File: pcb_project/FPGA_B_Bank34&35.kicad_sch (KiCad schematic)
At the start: 6 parts, among them U1 XC7A100T-FTG256, Y3 XLH736025.175000I

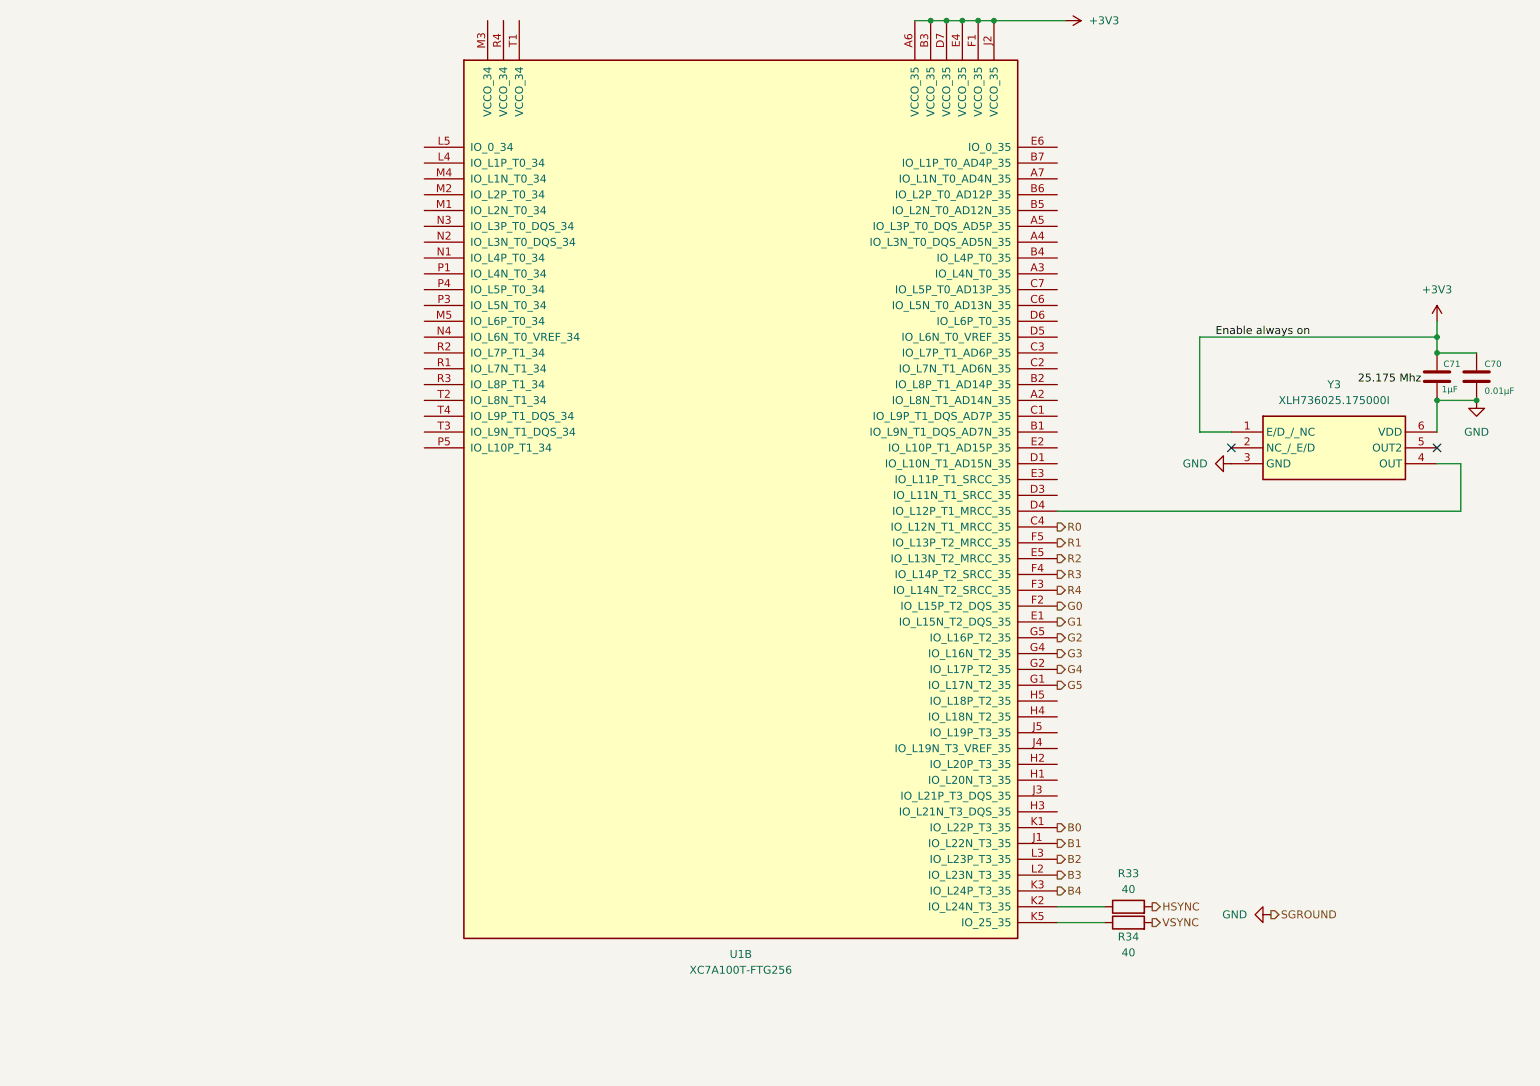
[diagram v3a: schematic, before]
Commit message: Add FPGA configuration LED's, config pins, no connect symbols
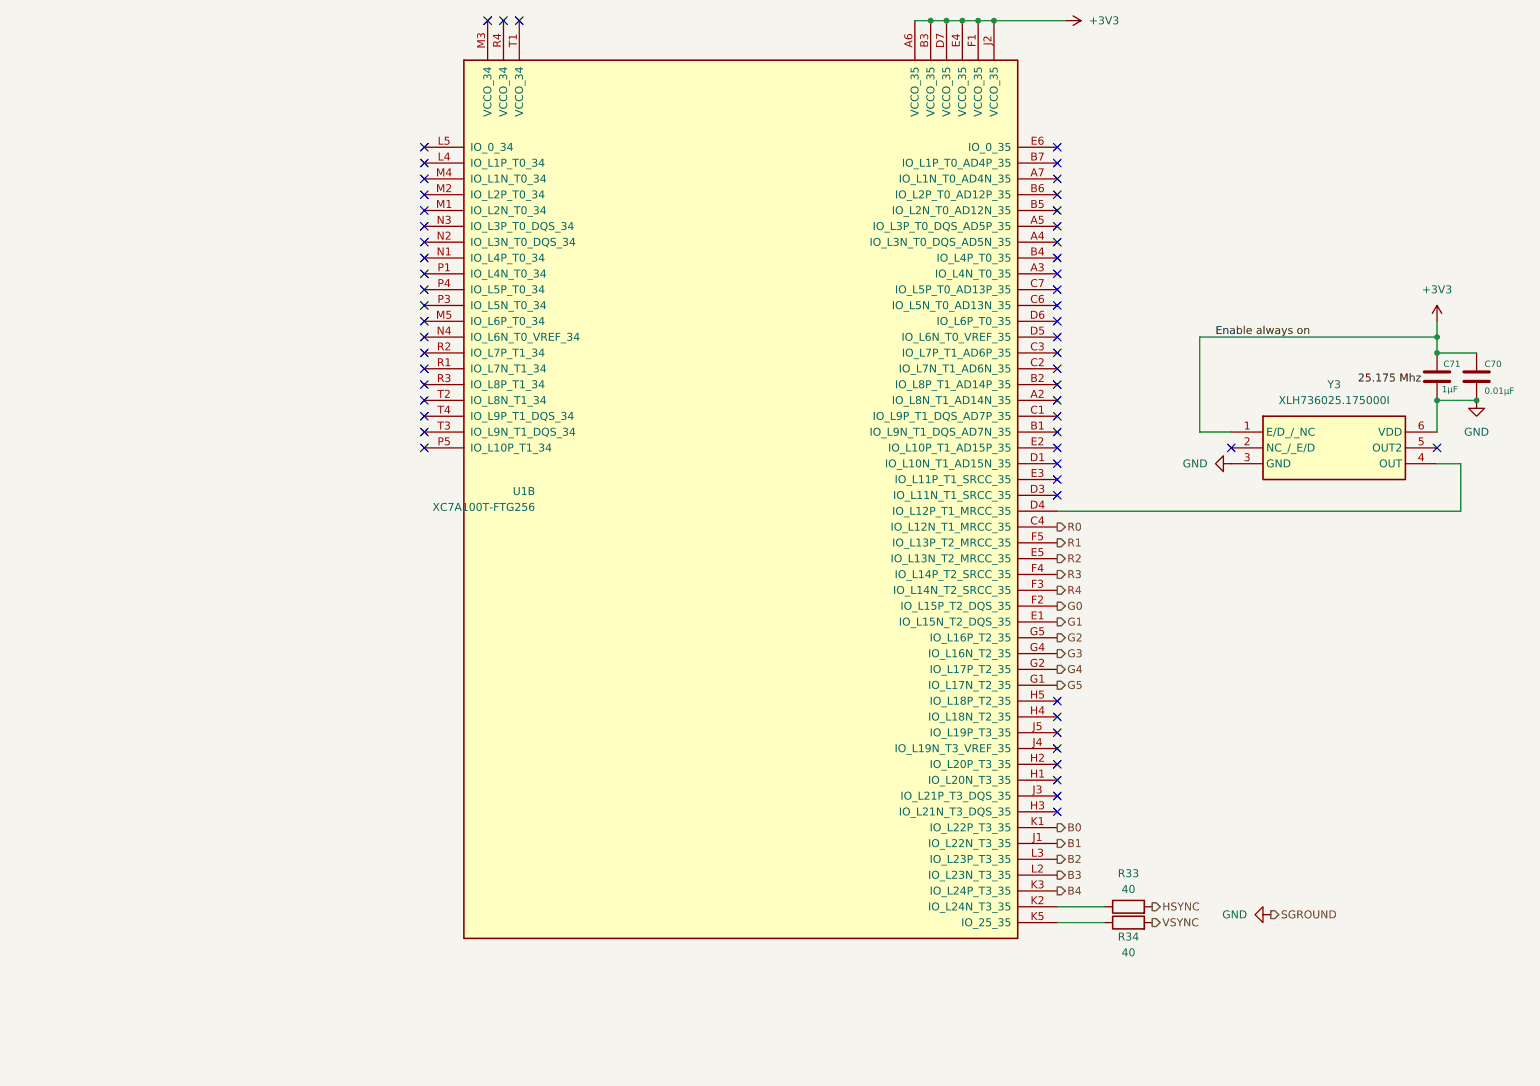
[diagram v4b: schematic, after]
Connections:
- no-connect marks 2 -> 56
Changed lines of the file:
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@@
+	)
+	(no_connect
+		(at 196.85 80.01)
+	)
+	(no_connect
+		(at 196.85 62.23)
+	)
+	(no_connect
+		(at 196.85 59.69)
+	)
+	(no_connect
+		(at 95.25 54.61)
+	)
+	(no_connect
+		(at 95.25 39.37)
+	)
+	(no_connect
+		(at 196.85 36.83)
+	)
+	(no_connect
+		(at 95.25 46.99)
+	)
+	(no_connect
+		(at 95.25 62.23)
+	)
+	(no_connect
+		(at 196.85 39.37)
+	)
+	(no_connect
+		(at 95.25 57.15)
+	)
+	(no_connect
+		(at 196.85 85.09)
+	)
+	(no_connect
+		(at 95.25 82.55)
+	)
+	(no_connect
+		(at 196.85 57.15)
+	)
+	(no_connect
+		(at 196.85 74.93)
+	)
+	(no_connect
+		(at 196.85 69.85)
+	)
+	(no_connect
+		(at 196.85 67.31)
+	)
+	(no_connect
+		(at 196.85 87.63)
+	)
+	(no_connect
+		(at 196.85 54.61)
+	)
+	(no_connect
+		(at 107.95 13.97)
+	)
+	(no_connect
+		(at 196.85 90.17)
+	)
+	(no_connect
+		(at 196.85 44.45)
+	)
+	(no_connect
+		(at 196.85 52.07)
+	)
+	(no_connect
+		(at 196.85 72.39)
+	)
+	(no_connect
+		(at 196.85 133.35)
+	)
+	(no_connect
+		(at 196.85 77.47)
+	)
+	(no_connect
+		(at 95.25 36.83)
+	)
+	(no_connect
+		(at 196.85 46.99)
+	)
+	(no_connect
+		(at 196.85 140.97)
+	)
+	(no_connect
+		(at 196.85 130.81)
+	)
+	(no_connect
+		(at 95.25 69.85)
+	)
+	(no_connect
+		(at 95.25 77.47)
+	)
+	(no_connect
+		(at 105.41 13.97)
 	)
 	(no_connect
@@
 	)
 	(no_connect
+		(at 196.85 49.53)
+	)
+	(no_connect
+		(at 196.85 128.27)
+	)
+	(no_connect
+		(at 196.85 34.29)
+	)
+	(no_connect
+		(at 196.85 64.77)
+	)
+	(no_connect
+		(at 196.85 135.89)
+	)
+	(no_connect
+		(at 95.25 72.39)
+	)
+	(no_connect
+		(at 95.25 59.69)
+	)
+	(no_connect
+		(at 196.85 41.91)
+	)
+	(no_connect
+		(at 95.25 80.01)
+	)
+	(no_connect
+		(at 196.85 123.19)
+	)
+	(no_connect
+		(at 95.25 49.53)
+	)
+	(no_connect
+		(at 196.85 125.73)
+	)
+	(no_connect
+		(at 95.25 34.29)
+	)
+	(no_connect
+		(at 95.25 64.77)
+	)
+	(no_connect
+		(at 196.85 82.55)
+	)
+	(no_connect
+		(at 95.25 74.93)
+	)
+	(no_connect
+		(at 95.25 67.31)
+	)
+	(no_connect
+		(at 110.49 13.97)
+	)
+	(no_connect
+		(at 196.85 138.43)
+	)
+	(no_connect
+		(at 95.25 44.45)
+	)
+	(no_connect
 		(at 224.79 82.55)
+	)
+	(no_connect
+		(at 95.25 41.91)
+	)
+	(no_connect
+		(at 95.25 52.07)
 	)
 	(wire
@@
 		(fields_autoplaced yes)
 		(property "Reference" "U1"
-			(at 146.05 163.83 0)
-			(effects
-				(font
-					(size 1.27 1.27)
-				)
+			(at 113.03 89.5349 0)
+			(effects
+				(font
+					(size 1.27 1.27)
+				)
+				(justify right)
 			)
 		)
 		(property "Value" "XC7A100T-FTG256"
-			(at 146.05 166.37 0)
-			(effects
-				(font
-					(size 1.27 1.27)
-				)
+			(at 113.03 92.0749 0)
+			(effects
+				(font
+					(size 1.27 1.27)
+				)
+				(justify right)
 			)
 		)
@@
 		)
 		(instances
-			(project "pcb_project"
+			(project ""
+				(path "/98f80f66-4595-4d0f-90ca-59b2db6f447b/8bdc4eb6-105b-4ccb-b86f-5b5221dfef47"
+					(reference "U1")
+					(unit 2)
+				)
 				(path "/98f80f66-4595-4d0f-90ca-59b2db6f447b/8bdc4eb6-105b-4ccb-b86f-5b5221dfef47/1311c77a-2e60-4e70-8492-84cf53095df7"
 					(reference "U1")

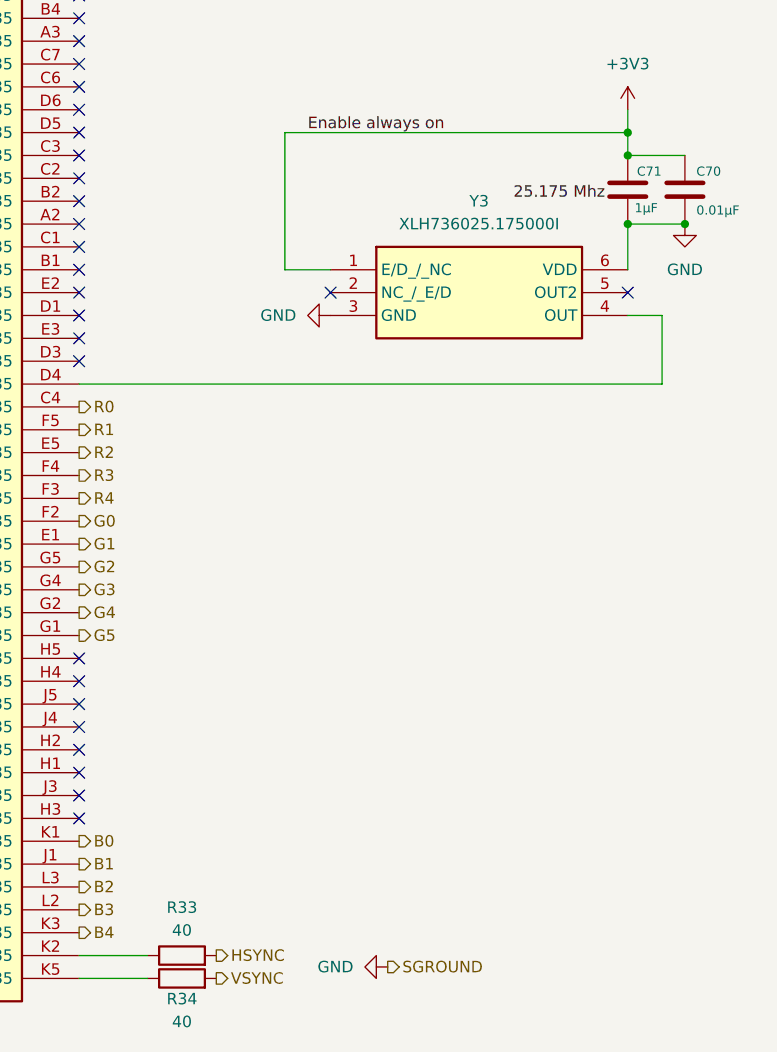
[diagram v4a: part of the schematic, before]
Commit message: ERC fixes, some remain
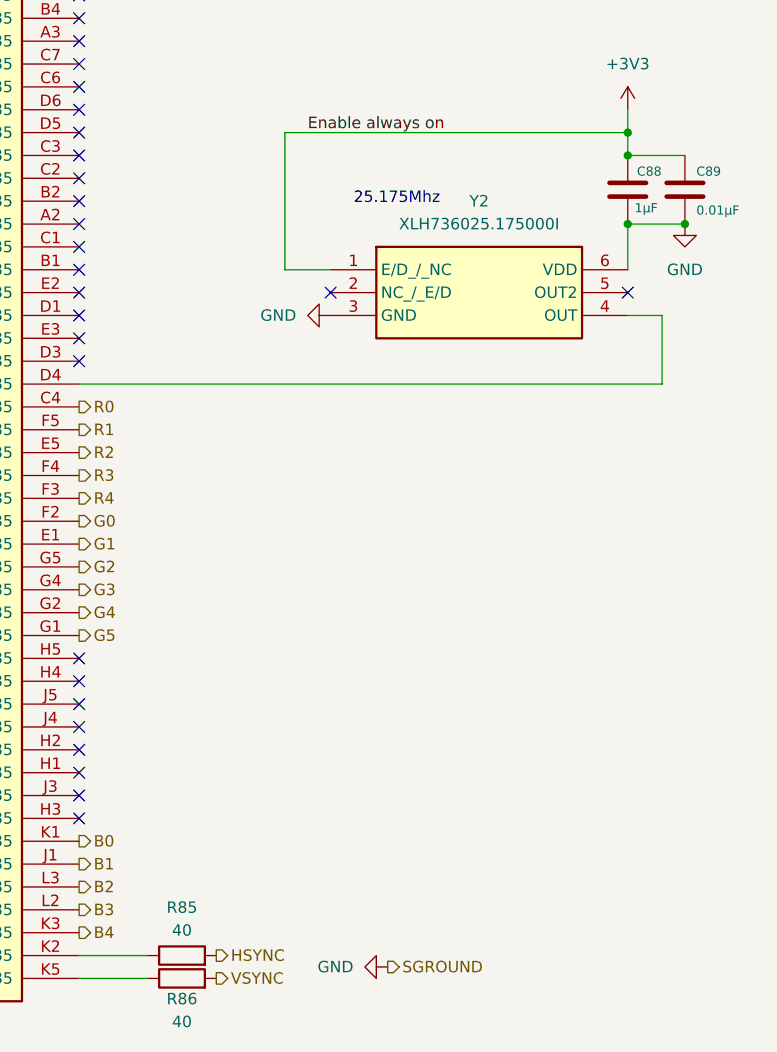
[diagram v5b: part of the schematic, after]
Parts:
- renumbered C71 to C88, C70 to C89, R33 to R85, R34 to R86, Y3 to Y2
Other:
- note added: "25.175Mhz"
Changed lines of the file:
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@@
 	(generator_version "9.0")
 	(paper "A4")
+	(text "25.175Mhz"
+		(exclude_from_sim no)
+		(at 232.156 72.136 0)
+		(effects
+			(font
+				(size 1.27 1.27)
+			)
+		)
+	)
 	(junction
 		(at 176.53 13.97)
@@
 			(width 0)
 			(type default)
-		)
-	)
-	(label "25.175 Mhz"
-		(at 245.11 72.39 0)
-		(effects
-			(font
-				(size 1.27 1.27)
-			)
-			(justify left bottom)
 		)
 	)
@@
 		(dnp no)
 		(fields_autoplaced yes)
-		(property "Reference" "#PWR014"
+		(property "Reference" "#PWR0116"
 			(at 218.44 85.09 0)
 			(effects
@@
 			(project ""
 				(path "/98f80f66-4595-4d0f-90ca-59b2db6f447b/8bdc4eb6-105b-4ccb-b86f-5b5221dfef47/1311c77a-2e60-4e70-8492-84cf53095df7"
-					(reference "#PWR014")
+					(reference "#PWR0116")
 					(unit 1)
 				)
@@
 		(dnp no)
 		(fields_autoplaced yes)
-		(property "Reference" "#PWR085"
+		(property "Reference" "#PWR0119"
 			(at 264.16 81.28 0)
 			(effects
@@
 			(project ""
 				(path "/98f80f66-4595-4d0f-90ca-59b2db6f447b/8bdc4eb6-105b-4ccb-b86f-5b5221dfef47/1311c77a-2e60-4e70-8492-84cf53095df7"
-					(reference "#PWR085")
+					(reference "#PWR0119")
 					(unit 1)
 				)
@@
 		(dnp no)
 		(fields_autoplaced yes)
-		(property "Reference" "#PWR017"
+		(property "Reference" "#PWR0118"
 			(at 257.81 66.04 0)
 			(effects
@@
 			(project ""
 				(path "/98f80f66-4595-4d0f-90ca-59b2db6f447b/8bdc4eb6-105b-4ccb-b86f-5b5221dfef47/1311c77a-2e60-4e70-8492-84cf53095df7"
-					(reference "#PWR017")
+					(reference "#PWR0118")
 					(unit 1)
 				)
@@
 		(dnp no)
 		(fields_autoplaced yes)
-		(property "Reference" "#PWR087"
+		(property "Reference" "#PWR0115"
 			(at 194.31 13.97 0)
 			(effects
@@
 			(project ""
 				(path "/98f80f66-4595-4d0f-90ca-59b2db6f447b/8bdc4eb6-105b-4ccb-b86f-5b5221dfef47/1311c77a-2e60-4e70-8492-84cf53095df7"
-					(reference "#PWR087")
+					(reference "#PWR0115")
 					(unit 1)
 				)
@@
 		(on_board yes)
 		(dnp no)
-		(property "Reference" "R33"
+		(property "Reference" "R85"
 			(at 208.28 150.876 90)
 			(effects
@@
 			(project ""
 				(path "/98f80f66-4595-4d0f-90ca-59b2db6f447b/8bdc4eb6-105b-4ccb-b86f-5b5221dfef47/1311c77a-2e60-4e70-8492-84cf53095df7"
-					(reference "R33")
+					(reference "R85")
 					(unit 1)
 				)
@@
 		(on_board yes)
 		(dnp no)
-		(property "Reference" "C70"
+		(property "Reference" "C89"
 			(at 265.43 69.088 0)
 			(effects
@@
 			(project ""
 				(path "/98f80f66-4595-4d0f-90ca-59b2db6f447b/8bdc4eb6-105b-4ccb-b86f-5b5221dfef47/1311c77a-2e60-4e70-8492-84cf53095df7"
-					(reference "C70")
+					(reference "C89")
 					(unit 1)
 				)
@@
 		(on_board yes)
 		(dnp no)
-		(property "Reference" "C71"
+		(property "Reference" "C88"
 			(at 258.826 69.088 0)
 			(effects
@@
 			(project "pcb_project"
 				(path "/98f80f66-4595-4d0f-90ca-59b2db6f447b/8bdc4eb6-105b-4ccb-b86f-5b5221dfef47/1311c77a-2e60-4e70-8492-84cf53095df7"
-					(reference "C71")
+					(reference "C88")
 					(unit 1)
 				)
@@
 		(on_board yes)
 		(dnp no)
-		(property "Reference" "R34"
+		(property "Reference" "R86"
 			(at 208.28 161.036 90)
 			(effects
@@
 			(project ""
 				(path "/98f80f66-4595-4d0f-90ca-59b2db6f447b/8bdc4eb6-105b-4ccb-b86f-5b5221dfef47/1311c77a-2e60-4e70-8492-84cf53095df7"
-					(reference "R34")
+					(reference "R86")
 					(unit 1)
 				)
@@
 		(dnp no)
 		(fields_autoplaced yes)
-		(property "Reference" "#PWR088"
+		(property "Reference" "#PWR0117"
 			(at 224.79 157.48 0)
 			(effects
@@
 			(project ""
 				(path "/98f80f66-4595-4d0f-90ca-59b2db6f447b/8bdc4eb6-105b-4ccb-b86f-5b5221dfef47/1311c77a-2e60-4e70-8492-84cf53095df7"
-					(reference "#PWR088")
+					(reference "#PWR0117")
 					(unit 1)
 				)
@@
 		(dnp no)
 		(fields_autoplaced yes)
-		(property "Reference" "Y3"
+		(property "Reference" "Y2"
 			(at 241.3 72.39 0)
 			(effects
@@
 			(project ""
 				(path "/98f80f66-4595-4d0f-90ca-59b2db6f447b/8bdc4eb6-105b-4ccb-b86f-5b5221dfef47/1311c77a-2e60-4e70-8492-84cf53095df7"
-					(reference "Y3")
+					(reference "Y2")
 					(unit 1)
 				)

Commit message: Fix JTAG connector, add pullups (FPGA has internal pullups as well), add some capacitor footprints
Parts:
- Y2: footprint XLH730003580000I -> Project_Footprints:XLH730003580000I
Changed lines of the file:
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@@
 			)
 		)
-		(property "Footprint" "XLH730003580000I"
+		(property "Footprint" "Project_Footprints:XLH730003580000I"
 			(at 254 174.93 0)
 			(effects

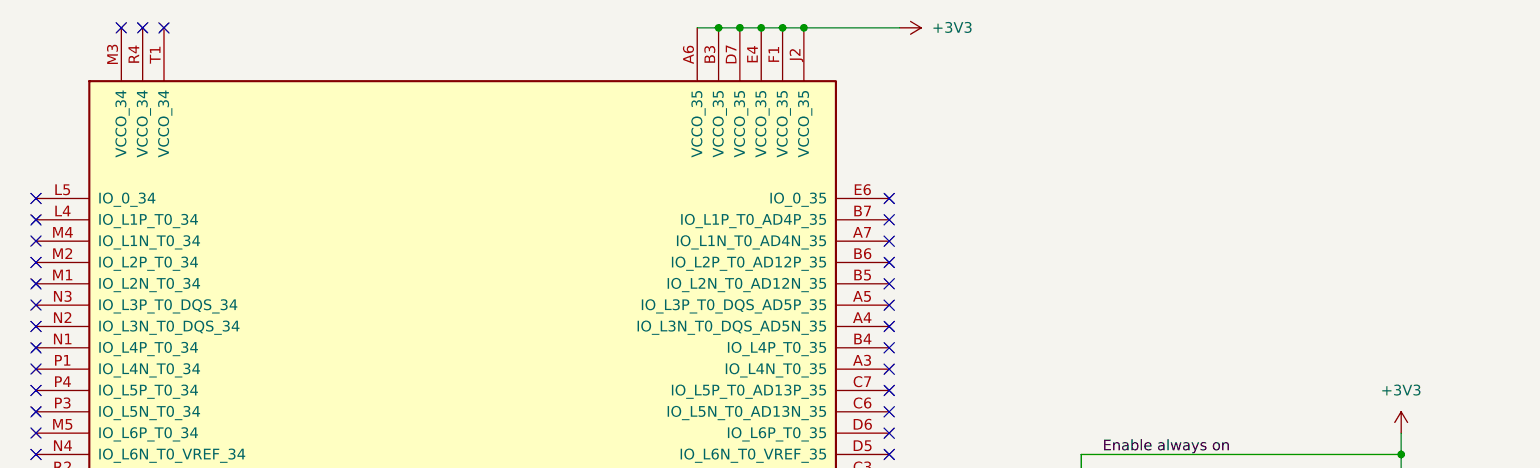
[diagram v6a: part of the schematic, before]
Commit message: Tied unused FGPA vcco to ground. Moved decoupling to all banks.
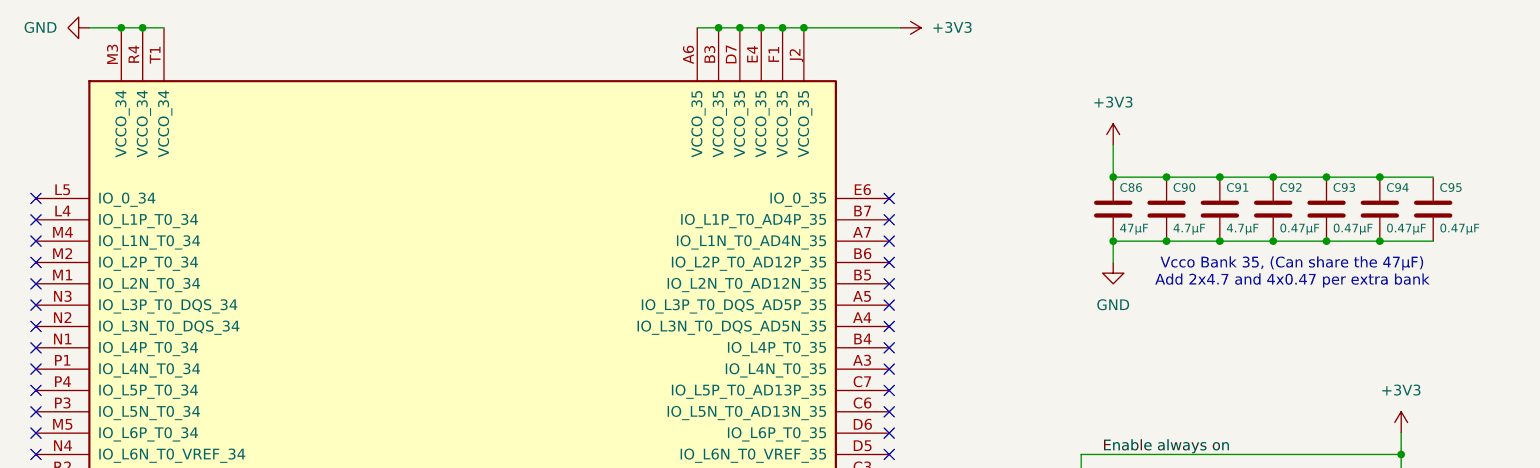
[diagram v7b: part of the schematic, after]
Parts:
- added C86: 47µF, Capacitor_SMD:C_1210_3225Metric_Pad1.33x2.70mm_HandSolder, symbol Device:C
- added C90, C91: 4.7µF, Capacitor_SMD:C_0805_2012Metric_Pad1.18x1.45mm_HandSolder, symbol Device:C
- added C92, C93, C94, C95: 0.47µF, Capacitor_SMD:C_0805_2012Metric_Pad1.18x1.45mm_HandSolder, symbol Device:C
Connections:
- net +3V3: now also C86.1, C90.1, C91.1, C92.1, C93.1, C94.1, C95.1
- net GND: now also U1.M3 (VCCO_34), U1.R4 (VCCO_34), U1.T1 (VCCO_34), C86.2, C90.2, C91.2, C92.2, C93.2, C94.2, C95.2
- no-connect marks 56 -> 53
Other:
- note added: "Vcco Bank 35, (Can share the 47µF) Add 2x4.7 and 4x0.47 per extra bank"

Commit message: Add most footprints, missing some inductors and 3 buttons
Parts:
- C88: footprint (none) -> Capacitor_SMD:C_0805_2012Metric_Pad1.18x1.45mm_HandSolder
- C89: footprint (none) -> Capacitor_SMD:C_0603_1608Metric_Pad1.08x0.95mm_HandSolder
- R85, R86: footprint (none) -> Resistor_SMD:R_0805_2012Metric_Pad1.20x1.40mm_HandSolder
- U1: footprint (none) -> Package_BGA:Xilinx_FTG256
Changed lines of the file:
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@@
 			)
 		)
-		(property "Footprint" ""
+		(property "Footprint" "Resistor_SMD:R_0805_2012Metric_Pad1.20x1.40mm_HandSolder"
 			(at 208.28 157.988 90)
 			(effects
@@
 			)
 		)
-		(property "Footprint" ""
+		(property "Footprint" "Capacitor_SMD:C_0603_1608Metric_Pad1.08x0.95mm_HandSolder"
 			(at 265.1252 74.93 0)
 			(effects
@@
 			)
 		)
-		(property "Footprint" ""
+		(property "Footprint" "Capacitor_SMD:C_0805_2012Metric_Pad1.18x1.45mm_HandSolder"
 			(at 258.7752 74.93 0)
 			(effects
@@
 			)
 		)
-		(property "Footprint" ""
+		(property "Footprint" "Package_BGA:Xilinx_FTG256"
 			(at 146.05 87.63 0)
 			(effects
@@
 			)
 		)
-		(property "Footprint" ""
+		(property "Footprint" "Resistor_SMD:R_0805_2012Metric_Pad1.20x1.40mm_HandSolder"
 			(at 208.28 160.528 90)
 			(effects
